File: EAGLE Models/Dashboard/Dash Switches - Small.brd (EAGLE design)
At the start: 25.7 x 15.2 mm, 14 parts

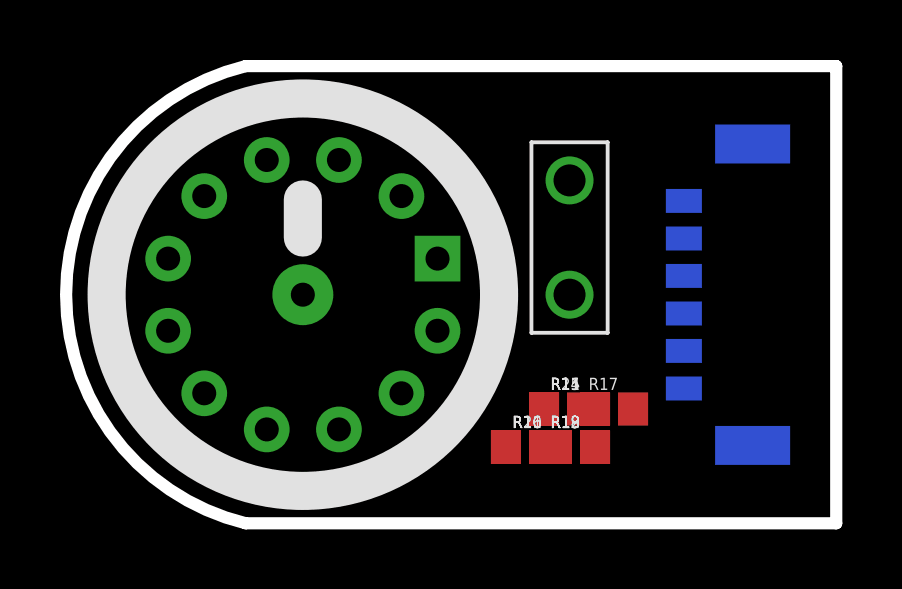
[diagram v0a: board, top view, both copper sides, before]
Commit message: Route single dash switch board.
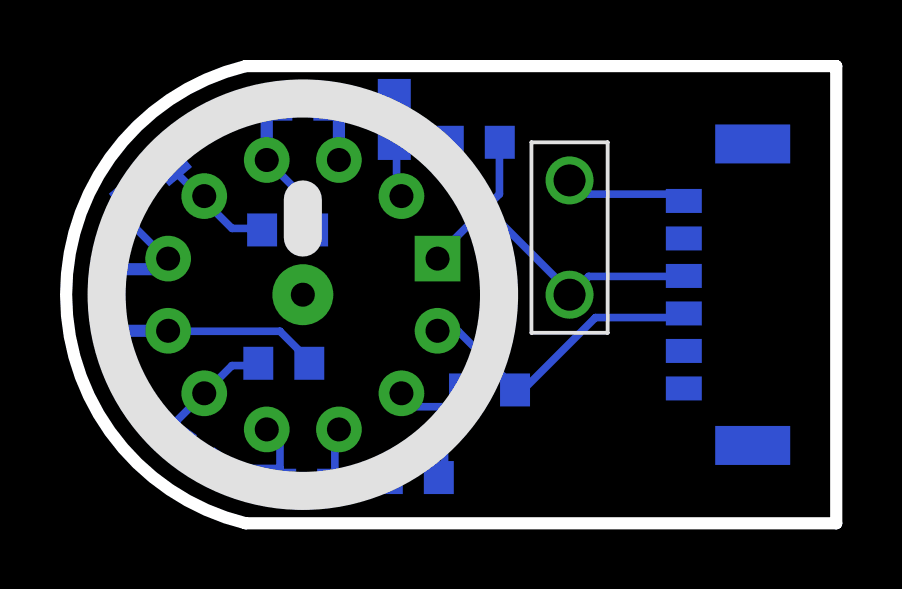
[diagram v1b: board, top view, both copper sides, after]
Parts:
- moved R17 17.0 mm to (2.54, 11.4), flipped to the bottom, turned to 140 degrees
- moved R16 15.0 mm to (1.14, 7.62), flipped to the bottom, turned to 90 degrees
- moved R19 14.5 mm to (7.62, 14.0), flipped to the bottom, turned to 180 degrees
- moved R14 12.5 mm to (4.06, 2.29), flipped to the bottom, turned to 35 degrees
- moved R18 11.9 mm to (7.11, 9.78), flipped to the bottom, turned to 180 degrees
- moved R20 11.8 mm to (10.7, 13.5), flipped to the bottom, turned to 270 degrees
- moved R15 9.65 mm to (6.99, 5.33), flipped to the bottom, turned to 180 degrees
- moved R21 9.44 mm to (13.3, 12.7), flipped to the bottom, turned to 180 degrees
- moved R13 8.85 mm to (7.75, 1.27), flipped to the bottom
- moved R12 5.31 mm to (11.3, 1.52), flipped to the bottom
- moved R11 2.36 mm to (13.8, 4.45), flipped to the bottom
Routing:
- net GND: track 0.00 -> 12.8 mm
- net VCC: track 0.00 -> 10.2 mm
- net N$16: track 0.00 -> 7.32 mm
- net N$6: track 0.00 -> 5.05 mm
- net N$15: track 0.00 -> 5.04 mm
- net N$17: track 0.00 -> 4.74 mm
- net N$18: track 0.00 -> 4.35 mm
- net N$10: track 0.00 -> 4.18 mm
- net N$13: track 0.00 -> 4.14 mm
- net N$40: track 0.00 -> 4.10 mm
- net N$14: track 0.00 -> 4.08 mm
- net N$7: track 0.00 -> 4.07 mm
- net N$20: track 0.00 -> 3.65 mm

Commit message: Replace connectors with vias for soldering.
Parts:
- removed U$3: MICRO6LOCK, DashAndCAN library:MICRO6LOCK
- JP1: value M02PTH2 -> (none); device SparkFun-Connectors:1X02_BIG -> SparkFun-Connectors:1X03
- moved JP1 7.19 mm to (22.6, 11.4), turned to 270 degrees
- moved R20 0.13 mm to (10.7, 13.3)
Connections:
- removed net N$30: U$3.P2
- removed net N$40: JP1.P$2, U$3.P1
- net GND: now also JP1.2; no longer JP1.P$1, U$3.P3
- net N$19: now also JP1.1
- net VCC: now also JP1.3; no longer U$3.P4
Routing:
- net N$19: track 0.00 -> 16.6 mm
- net N$40: track 4.10 -> 0.00 mm
- net VCC: track 10.2 -> 12.6 mm
- net GND: track 12.8 -> 15.2 mm
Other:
- board text added: "GND"
- board text added: "SIG"
- board text added: "VCC"
